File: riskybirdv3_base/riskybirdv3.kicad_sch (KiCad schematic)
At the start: 179 parts, among them IC1 PMW3901MB-TXQT, J1 USB_B_Micro, J10 Conn_01x05, J11 Conn_01x05, J18 Conn_01x05_MountingPin, J19 Conn_01x30_MountingPin, J2 Conn_01x05, J3 Conn_01x02, J4 Conn_01x02, J5 Conn_01x02, J6 Conn_01x02, J7 Conn_01x02, J8 USB_B_Micro, J9 Conn_01x05, Q1 SI2302, Q2 SI2302, Q3 SI2302, Q4 SI2302, Q8 BC847BDW1, SW1 SW_SPST, SW2 SW_SPST, SW3 SW_SPST, SW4 SW_SPST, U1 ADS7128IRTER, U10 TLV70018DCKR, U11 TPS54331D, U12 LP2985-3.0, U13 TPS2113A, U14 ESP32-C6-MINI-1/U, U3 BMI088, U4 MCP73831-2-OT, U6 FT2232HL-REEL, U7 TPS2113A, U8 FT231XS, U9 VL53L1CXV0FY1, Y1 f

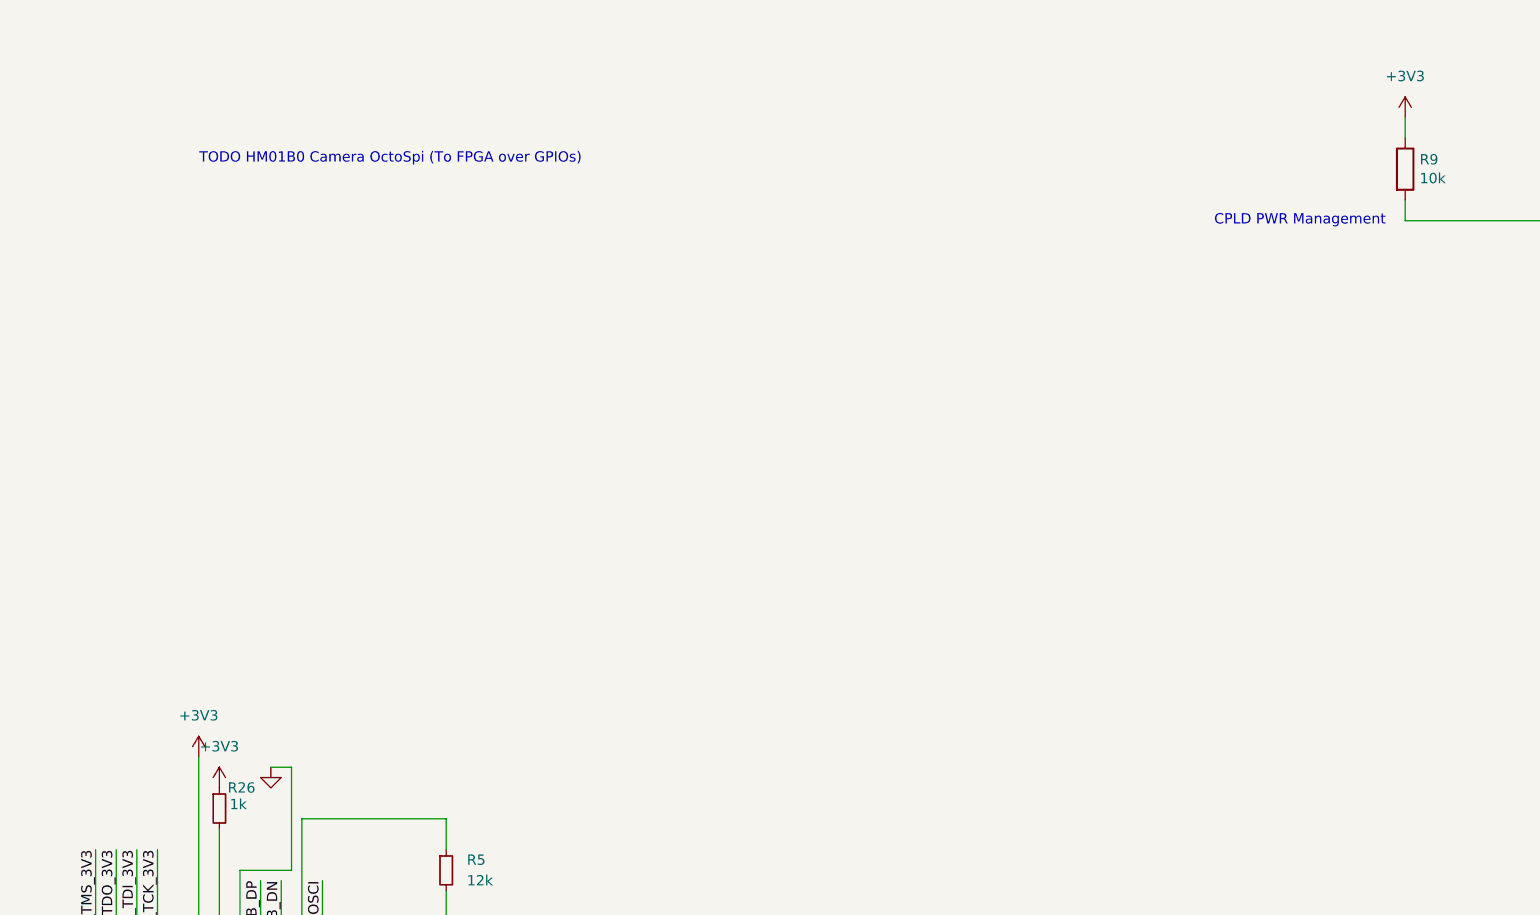
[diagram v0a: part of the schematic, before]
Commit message: update camera part
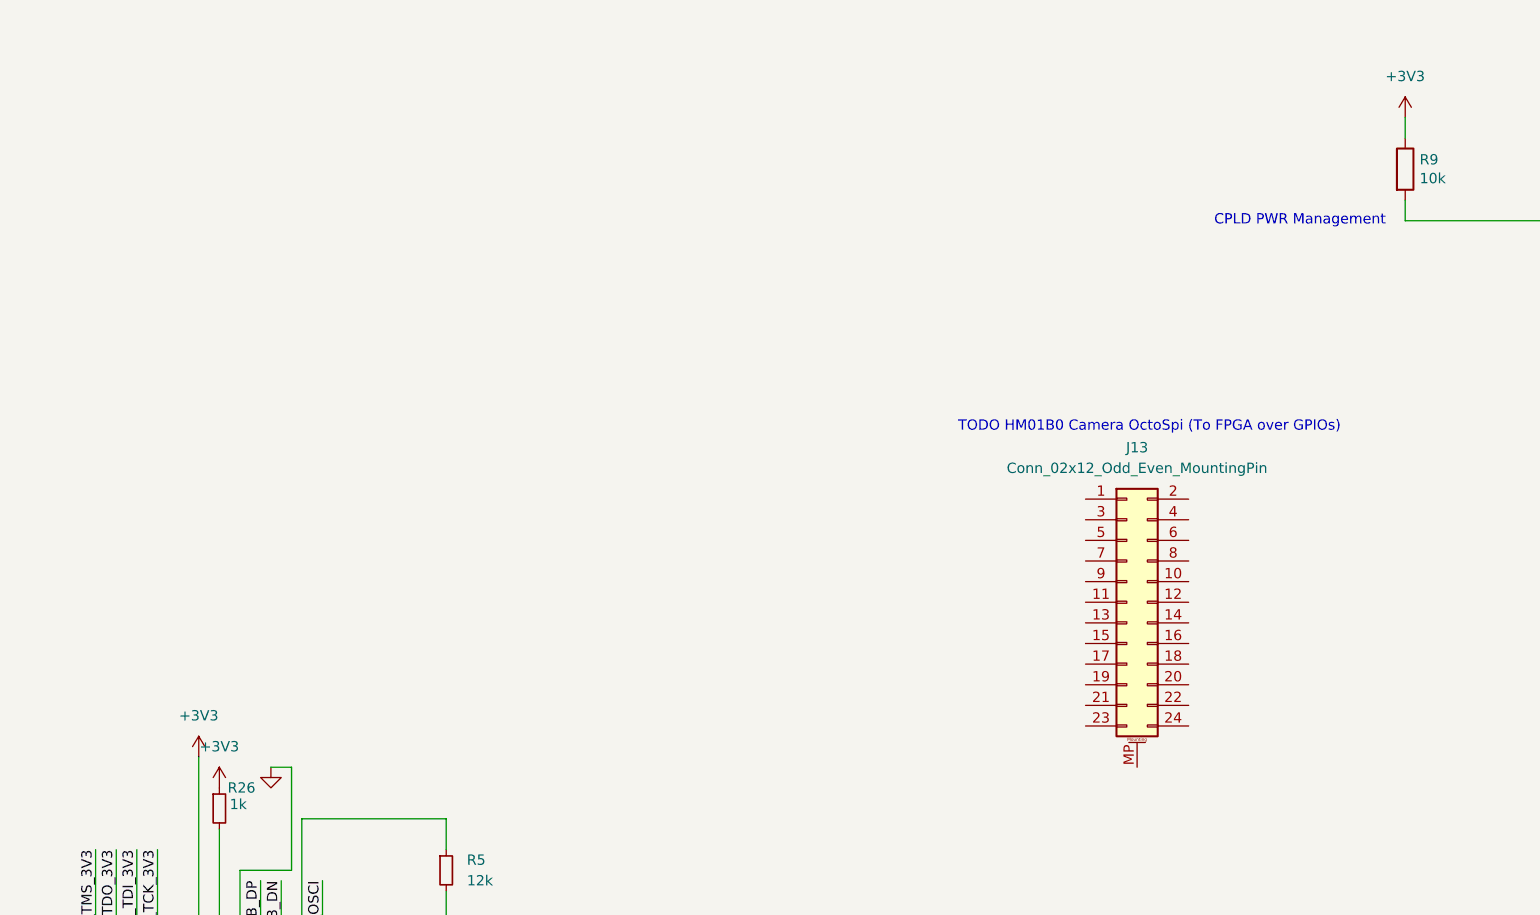
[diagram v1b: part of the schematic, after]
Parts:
- added J13: Conn_02x12_Odd_Even_MountingPin, riskybird:5037762410, symbol Connector_Generic_MountingPin:Conn_02x12_Odd_Even_MountingPin
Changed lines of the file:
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@@
 	(text "TODO HM01B0 Camera OctoSpi (To FPGA over GPIOs)"
 		(exclude_from_sim no)
-		(at 355.092 203.2 0)
+		(at 448.564 236.22 0)
 		(effects
 			(font
@@
 					(unit 1)
 				)
+			)
+		)
+	)
+	(symbol
+		(lib_id "Connector_Generic_MountingPin:Conn_02x12_Odd_Even_MountingPin")
+		(at 445.77 257.81 0)
+		(unit 1)
+		(body_style 1)
+		(exclude_from_sim no)
+		(in_bom yes)
+		(on_board yes)
+		(in_pos_files yes)
+		(dnp no)
+		(fields_autoplaced yes)
+		(property "Reference" "J13"
+			(at 447.04 238.76 0)
+			(show_name no)
+			(do_not_autoplace no)
+			(effects
+				(font
+					(size 1.27 1.27)
+				)
+			)
+		)
+		(property "Value" "Conn_02x12_Odd_Even_MountingPin"
+			(at 447.04 241.3 0)
+			(show_name no)
+			(do_not_autoplace no)
+			(effects
+				(font
+					(size 1.27 1.27)
+				)
+			)
+		)
+		(property "Footprint" "riskybird:5037762410"
+			(at 445.77 257.81 0)
+			(hide yes)
+			(show_name no)
+			(do_not_autoplace no)
+			(effects
+				(font
+					(size 1.27 1.27)
+				)
+			)
+		)
+		(property "Datasheet" ""
+			(at 445.77 257.81 0)
+			(hide yes)
+			(show_name no)
+			(do_not_autoplace no)
+			(effects
+				(font
+					(size 1.27 1.27)
+				)
+			)
+		)
+		(property "Description" "Generic connectable mounting pin connector, double row, 02x12, odd/even pin numbering scheme (row 1 odd numbers, row 2 even numbers), script generated (kicad-library-utils/schlib/autogen/connector/)"
+			(at 445.77 257.81 0)
+			(hide yes)
+			(show_name no)
+			(do_not_autoplace no)
+			(effects
+				(font
+					(size 1.27 1.27)
+				)
+			)
+		)
+		(pin "19"
+		)
+		(pin "11"
+		)
+		(pin "12"
+		)
+		(pin "5"
+		)
+		(pin "17"
+		)
+		(pin "10"
+		)
+		(pin "13"
+		)
+		(pin "3"
+		)
+		(pin "7"
+		)
+		(pin "4"
+		)
+		(pin "9"
+		)
+		(pin "6"
+		)
+		(pin "8"
+		)
+		(pin "20"
+		)
+		(pin "22"
+		)
+		(pin "23"
+		)
+		(pin "MP"
+		)
+		(pin "24"
+		)
+		(pin "21"
+		)
+		(pin "18"
+		)
+		(pin "14"
+		)
+		(pin "2"
+		)
+		(pin "1"
+		)
+		(pin "15"
+		)
+		(pin "16"
+		)
+		(instances
+			(project "riskybirdv3"
+				(path "/b045bc91-b5c2-4b45-9ee6-c32404600013"
+					(reference "J13")
+					(unit 1)
+				)
